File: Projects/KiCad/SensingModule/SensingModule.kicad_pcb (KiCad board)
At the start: 2 copper layers, 110 x 95 mm, 41 parts, among them J1 Conn_01x05_Socket, J2 Conn_01x02_Pin, J3 Conn_01x05_Pin, J4 Micro_SD_Card_Det_Hirose_DM3AT, Q1 DTC143E, U10 24LC1025, U11 24LC1025, U12 MB85RS2MT, U2 MCP2562-E-P, U3 NUCLEO-F303K8, U5 LT1584-3.3, U6 MB85RS2MT, U7 TLP222A, U8 24LC1025, U9 24LC1025

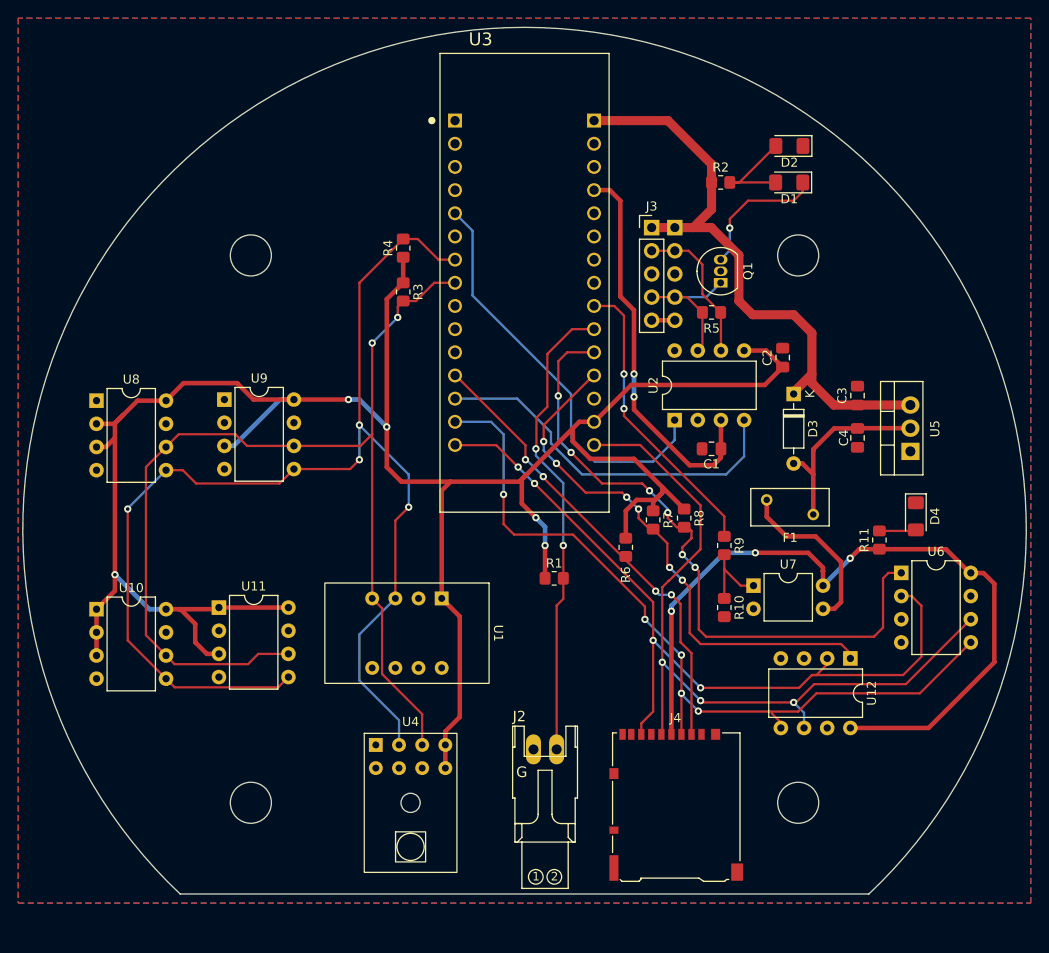
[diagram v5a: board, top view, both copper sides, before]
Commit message: 計測モジュールの基板設計概ね終わり
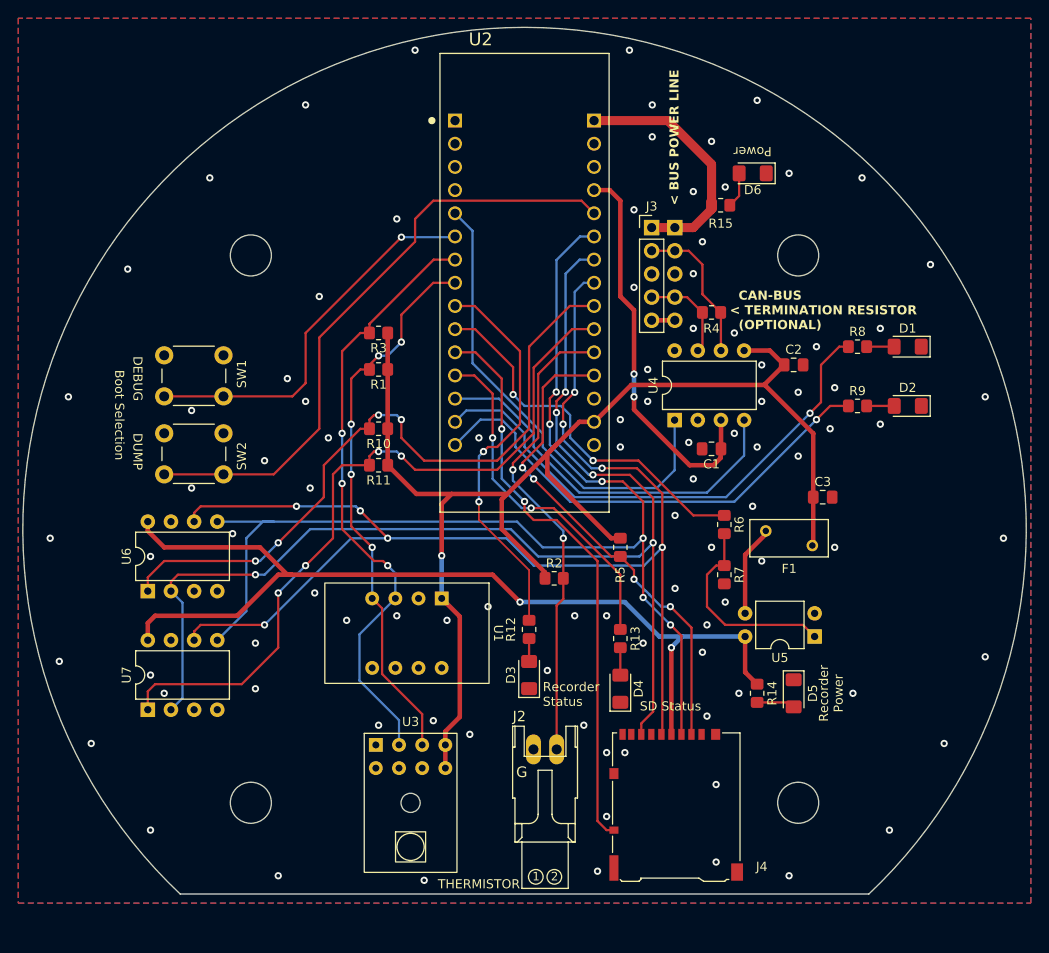
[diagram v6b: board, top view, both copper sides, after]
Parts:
- removed C4: 0.1μF, Capacitor_SMD:C_0805_2012Metric_Pad1.18x1.45mm_HandSolder
- removed Q1: DTC143E, Package_TO_SOT_THT:TO-92_Inline
- removed U10, U11, U8, U9: 24LC1025, Package_DIP:DIP-8_W7.62mm
- removed the U5 at (190.8, 96.5)
- added D2: LED, LED_SMD:LED_1206_3216Metric_Pad1.42x1.75mm_HandSolder, F.Cu at (190.5, 91.5)
- added D4: LED, LED_SMD:LED_1206_3216Metric_Pad1.42x1.75mm_HandSolder, F.Cu at (159.0, 122.5)
- added R12: 100Ω, Resistor_SMD:R_0805_2012Metric_Pad1.20x1.40mm_HandSolder, F.Cu at (149.0, 116.0)
- added R13: 100Ω, Resistor_SMD:R_0805_2012Metric_Pad1.20x1.40mm_HandSolder, F.Cu at (159.0, 117.0)
- added R8: 100Ω, Resistor_SMD:R_0805_2012Metric_Pad1.20x1.40mm_HandSolder, F.Cu at (185.0, 85.0)
- added R9: 100Ω, Resistor_SMD:R_0805_2012Metric_Pad1.20x1.40mm_HandSolder, F.Cu at (185.0, 91.5)
- added SW1: SW_Push, Button_Switch_THT:SW_PUSH_6mm, F.Cu at (109.0, 86.0)
- added SW2: SW_Push, Button_Switch_THT:SW_PUSH_6mm, F.Cu at (109.0, 94.5)
- C3: value 0.1μF -> 44μF
- D3: value 1N4148 -> LED; footprint Diode_THT:D_DO-35_SOD27_P7.62mm_Horizontal -> LED_SMD:LED_1206_3216Metric_Pad1.42x1.75mm_HandSolder
- moved U7 84.0 mm to (107.2, 124.8), turned to 90 degrees
- moved U6 77.4 mm to (107.2, 111.8), turned to 90 degrees
- moved D3 42.3 mm to (149.0, 121.0), turned to 90 degrees
- moved R10 34.9 mm to (132.5, 94.0), turned to 180 degrees
- moved R11 30.7 mm to (132.5, 98.0), turned to 180 degrees
- moved D5 23.6 mm to (178.0, 123.0)
- moved D1 22.2 mm to (190.5, 85.0)
- moved R14 21.5 mm to (174.0, 123.0), turned to -90 degrees
- moved C3 11.8 mm to (181.2, 101.5), turned to 0 degrees
- moved R3 9.68 mm to (132.5, 83.5), turned to 180 degrees
- moved R1 8.92 mm to (132.5, 87.5), turned to 180 degrees
- moved U5 8.72 mm to (180.3, 116.8), turned to 180 degrees
- moved D6 5.02 mm to (173.5, 66.0)
- moved R7 3.60 mm to (170.4, 110.0)
- moved F1 3.40 mm to (180.1, 106.8)
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- renumbered D4 to D5, D2 to D6, R3 to R1, R8 to R10, R7 to R11, R11 to R14, R2 to R15, R1 to R2, R4 to R3, R5 to R4, R6 to R5, R9 to R6, R10 to R7, U3 to U2, U4 to U3, U2 to U4, U7 to U5, U12 to U6, U6 to U7
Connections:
- C3 pad 1: +12V -> +3.3V
- D1 pad 1: Net-(D1-K) -> GND
- D3 pad 1: +12V -> GND
- D6 pad 2: Net-(D1-A) -> Net-(D6-A)
- F1 pad 1: Net-(D3-A) -> +3.3V
- J4 pad 10: unconnected-(J4-DET_A-Pad10) -> SD_CHECK
- J4 pad 9: unconnected-(J4-DET_B-Pad9) -> GND
- R10 pad 2: SPI_CS_FRAM0 -> SPI_CS_FRAM1
- R11 pad 2: SPI_CS_FRAM1 -> SPI_CS_FRAM0
- R15 pad 2: Net-(D1-A) -> Net-(D6-A)
- U2 pad 3_10: unconnected-(U3A-PF0-Pad3_10) -> MEMORY_POWER_CONTROL
- U2 pad 3_11: unconnected-(U3A-PF1-Pad3_11) -> SD_CHECK
- U2 pad 3_12: SPI_CS_SD -> SD_STATUS
- U2 pad 3_14: SPI_MOSI -> CAN_RECEIVE_STATUS
- U2 pad 3_15: SPI_MISO -> CAN_SEND_STATUS
- U2 pad 3_6: unconnected-(U3A-PB0-Pad3_6) -> DEBUG_MODE
- U2 pad 3_9: unconnected-(U3A-PB1-Pad3_9) -> RECORD_STATUS
- U2 pad 4_10: THERMISTOR -> SPI_CS_FRAM0
- U2 pad 4_11: SPI_CS_FRAM0 -> THERMISTOR
- U2 pad 4_12: SPI_CS_FRAM1 -> SPI_CS_SD
- U2 pad 4_15: SPI_SCLK -> unconnected-(U2B-PB3-Pad4_15)
- U2 pad 4_5: unconnected-(U3B-PA2-Pad4_5) -> DUMP_MODE
- U2 pad 4_6: unconnected-(U3B-PA7-Pad4_6) -> SPI_MOSI
- U2 pad 4_7: unconnected-(U3B-PA6-Pad4_7) -> SPI_MISO
- U2 pad 4_8: unconnected-(U3B-PA5-Pad4_8) -> SPI_SCLK
- U2 pad 4_9: MEMORY_POWER_CONTROL -> SPI_CS_FRAM1
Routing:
- net +3.3V: track 254.9 -> 147.8 mm, vias 5 -> 1
- net I2C_SDA: track 137.6 -> 66.7 mm, vias 4 -> 3
- net DUMP_MODE: track 0.00 -> 67.4 mm
- net SD_CHECK: track 0.00 -> 62.8 mm, vias 0 -> 2
- net I2C_SCL: track 122.0 -> 60.7 mm, vias 2 -> 5
- net CAN_RECEIVE_STATUS: track 0.00 -> 57.7 mm, vias 0 -> 1
- net SPI_SCLK: track 83.9 -> 141.4 mm, vias 3 -> 8
- net CAN_SEND_STATUS: track 0.00 -> 53.2 mm, vias 0 -> 1
- net SPI_MISO: track 87.9 -> 134.4 mm, vias 4 -> 5
- net RECORD_STATUS: track 0.00 -> 43.4 mm, vias 0 -> 2
- net SPI_MOSI: track 87.9 -> 130.3 mm, vias 5 -> 6
- net DEBUG_MODE: track 0.00 -> 42.4 mm, vias 0 -> 1
- net +12V: track 68.1 -> 27.2 mm
- net SD_STATUS: track 0.00 -> 38.6 mm, vias 0 -> 2
- net MEMORY_POWER: track 85.2 -> 108.2 mm, vias 3 -> 2
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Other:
- board text added: "< BUS POWER LINE"
- board text added: "Boot Selection"
- board text added: "CAN-BUS < TERMINATION RESISTOR (OPTIONAL)"
- board text added: "DEBUG"
- board text added: "DUMP"
- board text added: "Power"
- board text added: "Recorder Power"
- board text added: "Recorder Status"
- board text added: "SD Status"
- board text added: "THERMISTOR"

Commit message: 計測モジュールとフライトモジュール終わり
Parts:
- C3: value 44μF -> 470μF; footprint Capacitor_SMD:C_0805_2012Metric_Pad1.18x1.45mm_HandSolder -> Capacitor_THT:CP_Radial_D10.0mm_P3.50mm
- U3: footprint StrawberryLinux_LPS33HW_Module:LPS33HW -> Akizuki_BME280_Module:BME280
- moved U3 8.96 mm to (143.3, 140.1), turned to 180 degrees
- moved J2 5.04 mm to (150.8, 138.0)
- moved C3 3.77 mm to (184.4, 99.5)
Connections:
- U3 pad 1: GND -> +3.3V
- U3 pad 2: I2C_SDA -> GND
- U3 pad 3: I2C_SCL -> +3.3V
- U3 pad 4: +3.3V -> I2C_SDA
- U3 pad 6: unconnected-(U3-INT_DRDY-Pad6) -> I2C_SCL
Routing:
- net +3.3V: track 147.8 -> 159.6 mm
- net THERMISTOR: track 52.0 -> 57.0 mm
- net I2C_SCL: track 60.7 -> 63.4 mm
- net I2C_SDA: track 66.7 -> 69.3 mm
- net GND: vias 97 -> 100
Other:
- board text added: "CAN"
- board text added: "RECEIVE"
- board text added: "SEND"

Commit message: アルミ殿下を導電性高分子アルミ固体電解コンデンサに変更
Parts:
- C3: value 470μF -> 100μF; footprint Capacitor_THT:CP_Radial_D10.0mm_P3.50mm -> Capacitor_SMD:CP_Elec_6.3x7.7
- R1, R3: value 2.2kΩ -> 10kΩ
- moved C3 2.47 mm to (186.8, 99.0)
